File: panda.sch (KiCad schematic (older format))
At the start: 26 parts, among them J1 USB, J2 ICSP, U1 ATMEGA328-P, U2 MAX7219, Y1 12MHz

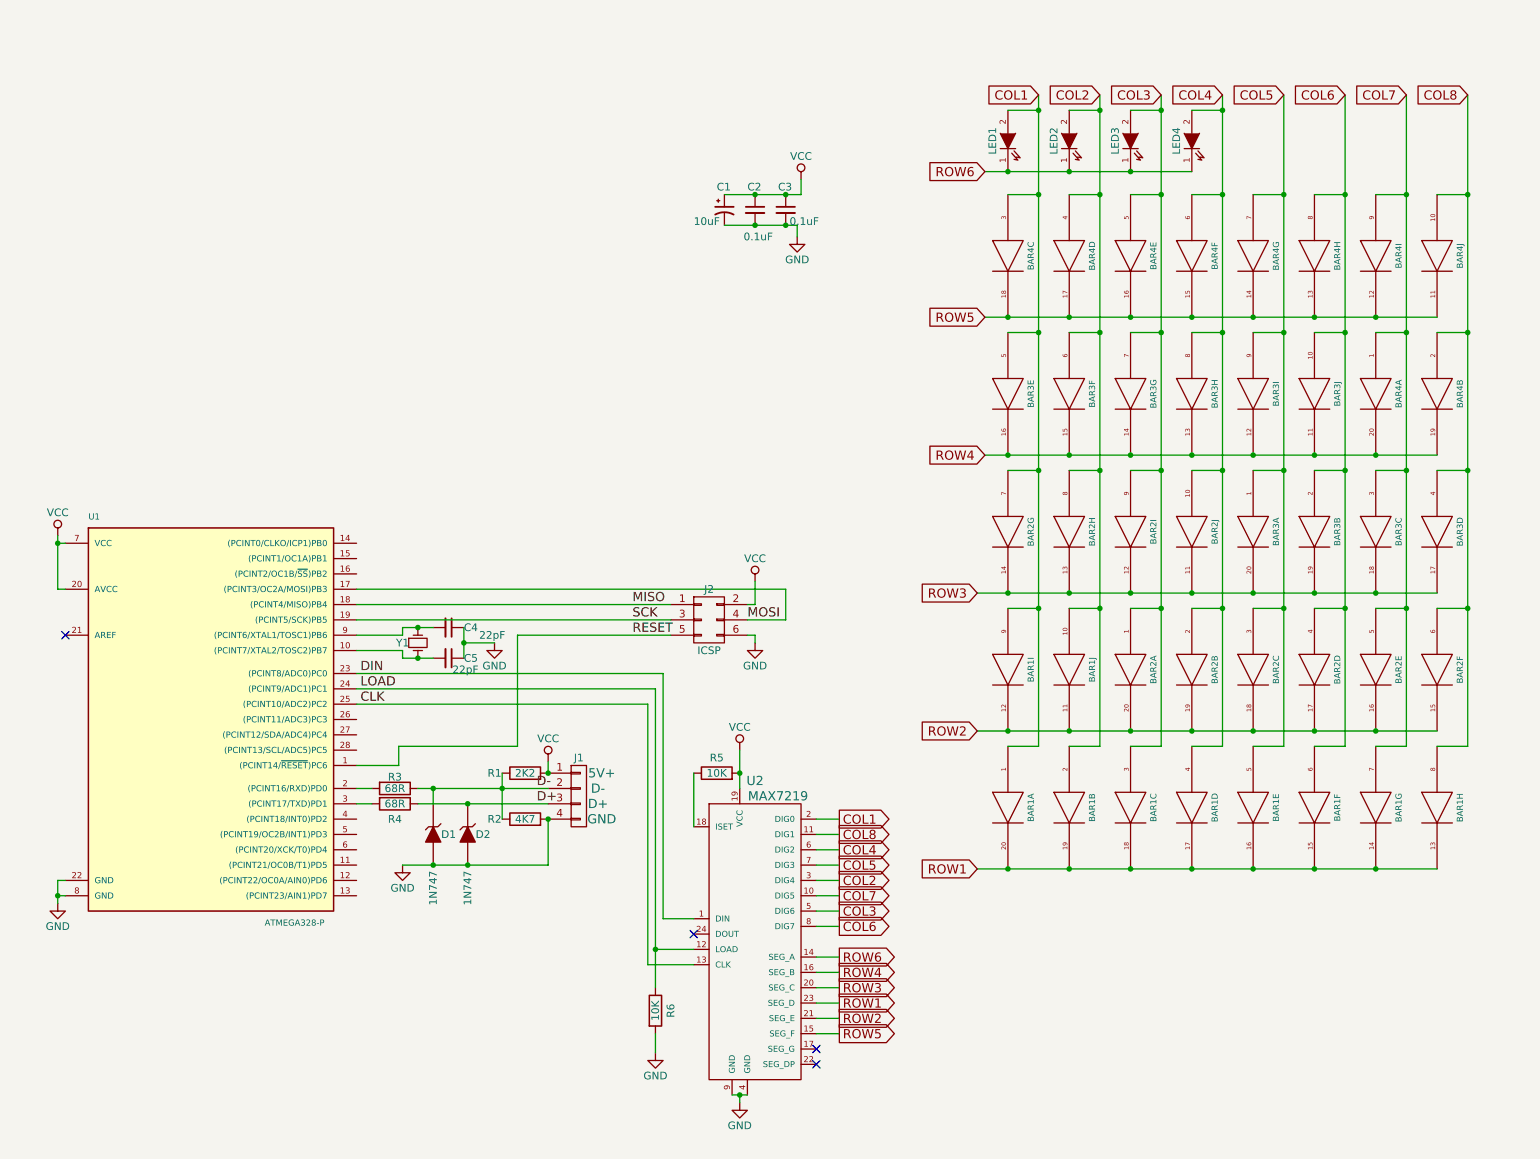
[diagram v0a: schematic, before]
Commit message: Variant with two rows of LED bars.
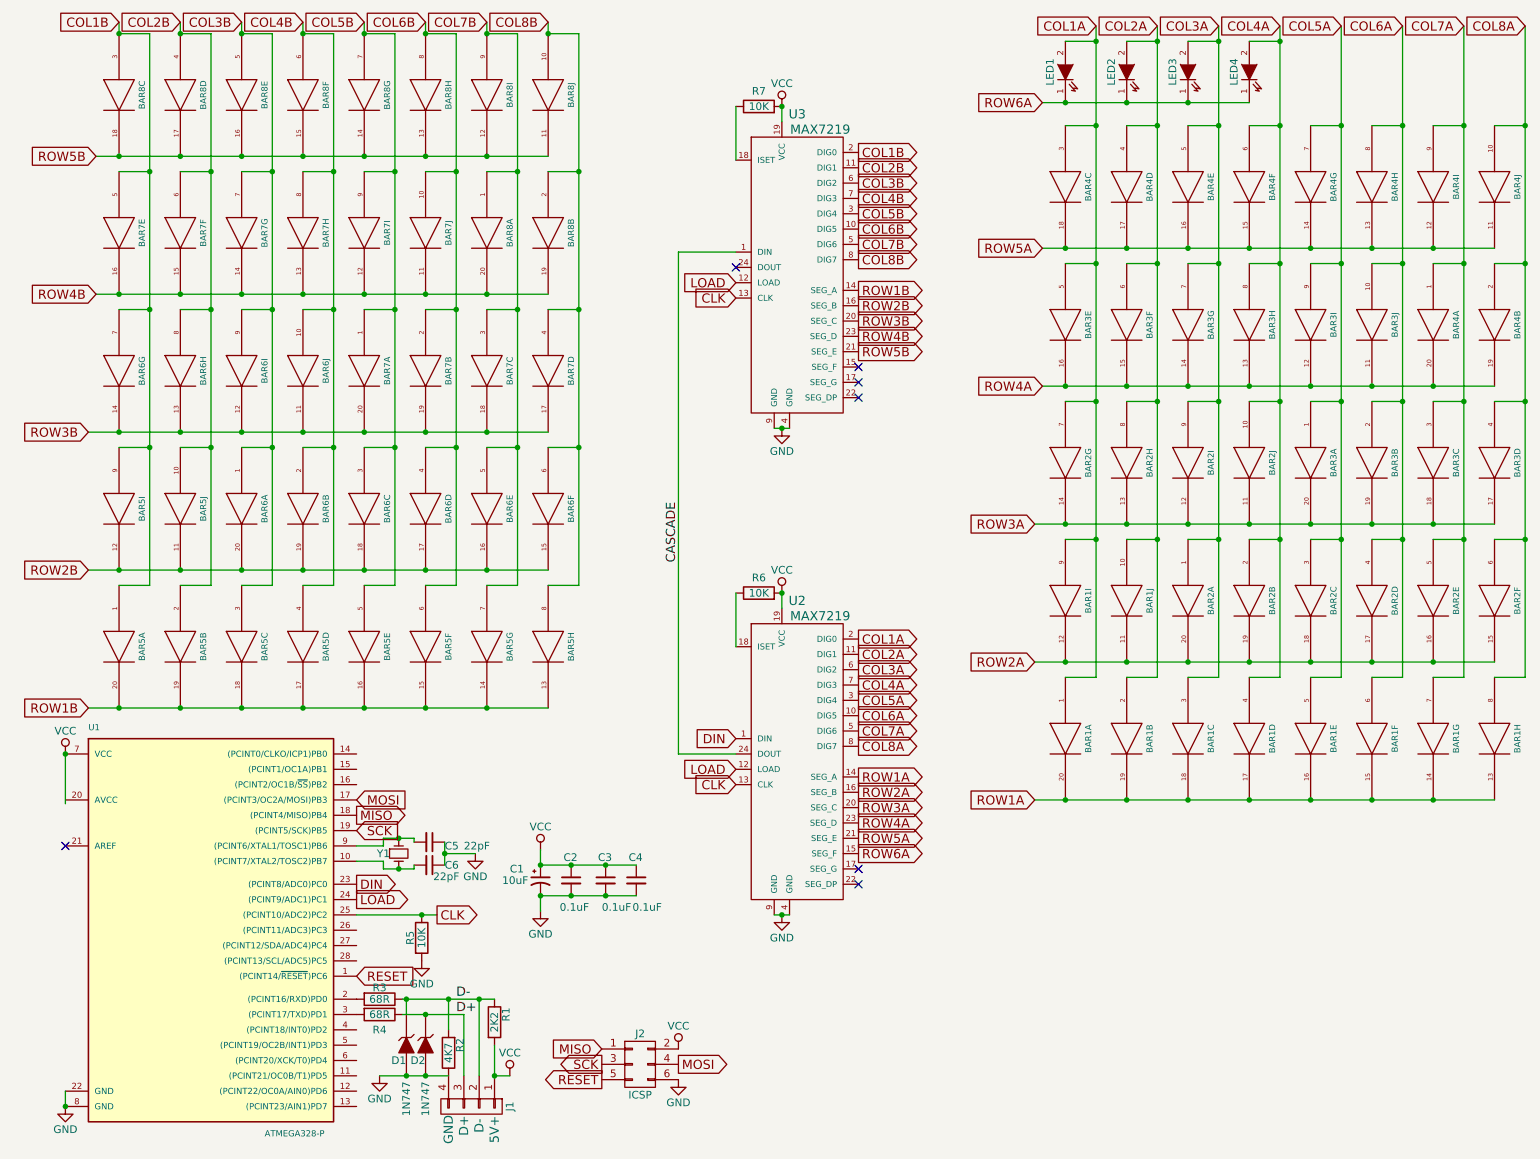
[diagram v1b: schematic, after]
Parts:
- added BAR5, BAR6, BAR7, BAR8: DOT-BAR, Housings_DIP:DIP-20_W7.62mm, symbol DOT-BAR
- added C4: 0.1uF, Capacitors_ThroughHole:C_Rect_L4_W2.5_P2.5, symbol C_Small
- added R7: 10K, custom_resistors:Resistor_Horizontal_RM7.62mm, symbol R
- added U3: MAX7219, Housings_DIP:DIP-24_W7.62mm, symbol MAX7219
- renumbered C4 to C5, C5 to C6, R6 to R5, R5 to R6
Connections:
- net CLK: now also R5.1, U3.13 (CLK)
- net D-: now also R2.2; no longer R2.1
- net GND: now also R2.1, C4.2, U3.4 (GND), U3.9 (GND); no longer R2.2
- net LOAD: now also U3.12 (LOAD); no longer R5.1
- net VCC: now also C4.1, R7.2, U3.19 (VCC); no longer U1.20 (AVCC)
- net CASCADE: now reaches U2.24 (DOUT)
- net CASCADE: now also U3.1 (DIN)
- net COL1 renamed COL1A
- net COL2 renamed COL2A
- net COL2A: now also U2.11 (DIG1); no longer U2.3 (DIG4)
- net COL3 renamed COL3A
- net COL3A: now also U2.6 (DIG2); no longer U2.5 (DIG6)
- net COL4 renamed COL4A
- net COL4A: now also U2.7 (DIG3); no longer U2.6 (DIG2)
- net COL5 renamed COL5A
- net COL5A: now also U2.3 (DIG4); no longer U2.7 (DIG3)
- net COL6 renamed COL6A
- net COL6A: now also U2.10 (DIG5); no longer U2.8 (DIG7)
- net COL7 renamed COL7A
- net COL7A: now also U2.5 (DIG6); no longer U2.10 (DIG5)
- net COL8 renamed COL8A
- net COL8A: now also U2.8 (DIG7); no longer U2.11 (DIG1)
- net ROW1 renamed ROW1A
- net ROW1A: now also U2.14 (SEG_A); no longer U2.23 (SEG_D)
- net ROW2 renamed ROW2A
- net ROW2A: now also U2.16 (SEG_B); no longer U2.21 (SEG_E)
- net ROW3 renamed ROW3A
- net ROW4 renamed ROW4A
- net ROW4A: now also U2.23 (SEG_D); no longer U2.16 (SEG_B)
- net ROW5 renamed ROW5A
- net ROW5A: now also U2.21 (SEG_E); no longer U2.15 (SEG_F)
- net ROW6 renamed ROW6A
- net ROW6A: now also U2.15 (SEG_F); no longer U2.14 (SEG_A)
- new net: R7.1, U3.18 (ISET)
- new net COL1B: BAR5.1 (A), BAR5.9 (A), BAR6.7 (A), BAR7.5 (A), BAR8.3 (A), U3.2 (DIG0)
- new net COL2B: BAR5.10 (A), BAR5.2 (A), BAR6.8 (A), BAR7.6 (A), BAR8.4 (A), U3.11 (DIG1)
- new net COL3B: BAR5.3 (A), BAR6.1 (A), BAR6.9 (A), BAR7.7 (A), BAR8.5 (A), U3.6 (DIG2)
- new net COL4B: BAR5.4 (A), BAR6.10 (A), BAR6.2 (A), BAR7.8 (A), BAR8.6 (A), U3.7 (DIG3)
- new net COL5B: BAR5.5 (A), BAR6.3 (A), BAR7.1 (A), BAR7.9 (A), BAR8.7 (A), U3.3 (DIG4)
- new net COL6B: BAR5.6 (A), BAR6.4 (A), BAR7.10 (A), BAR7.2 (A), BAR8.8 (A), U3.10 (DIG5)
- new net COL7B: BAR5.7 (A), BAR6.5 (A), BAR7.3 (A), BAR8.1 (A), BAR8.9 (A), U3.5 (DIG6)
- new net COL8B: BAR5.8 (A), BAR6.6 (A), BAR7.4 (A), BAR8.10 (A), BAR8.2 (A), U3.8 (DIG7)
- new net ROW1B: BAR5.13 (K), BAR5.14 (K), BAR5.15 (K), BAR5.16 (K), BAR5.17 (K), BAR5.18 (K), BAR5.19 (K), BAR5.20 (K), U3.14 (SEG_A)
- new net ROW2B: BAR5.11 (K), BAR5.12 (K), BAR6.15 (K), BAR6.16 (K), BAR6.17 (K), BAR6.18 (K), BAR6.19 (K), BAR6.20 (K), U3.16 (SEG_B)
- new net ROW3B: BAR6.11 (K), BAR6.12 (K), BAR6.13 (K), BAR6.14 (K), BAR7.17 (K), BAR7.18 (K), BAR7.19 (K), BAR7.20 (K), U3.20 (SEG_C)
- new net ROW4B: BAR7.11 (K), BAR7.12 (K), BAR7.13 (K), BAR7.14 (K), BAR7.15 (K), BAR7.16 (K), BAR8.19 (K), BAR8.20 (K), U3.23 (SEG_D)
- new net ROW5B: BAR8.11 (K), BAR8.12 (K), BAR8.13 (K), BAR8.14 (K), BAR8.15 (K), BAR8.16 (K), BAR8.17 (K), BAR8.18 (K), U3.21 (SEG_E)
- no-connect marks 4 -> 7
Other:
- moved on the sheet: BAR1A, BAR1B, BAR1C, BAR1D, BAR1E, BAR1F, BAR1G, BAR1H, BAR1I, BAR1J, BAR2A, BAR2B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

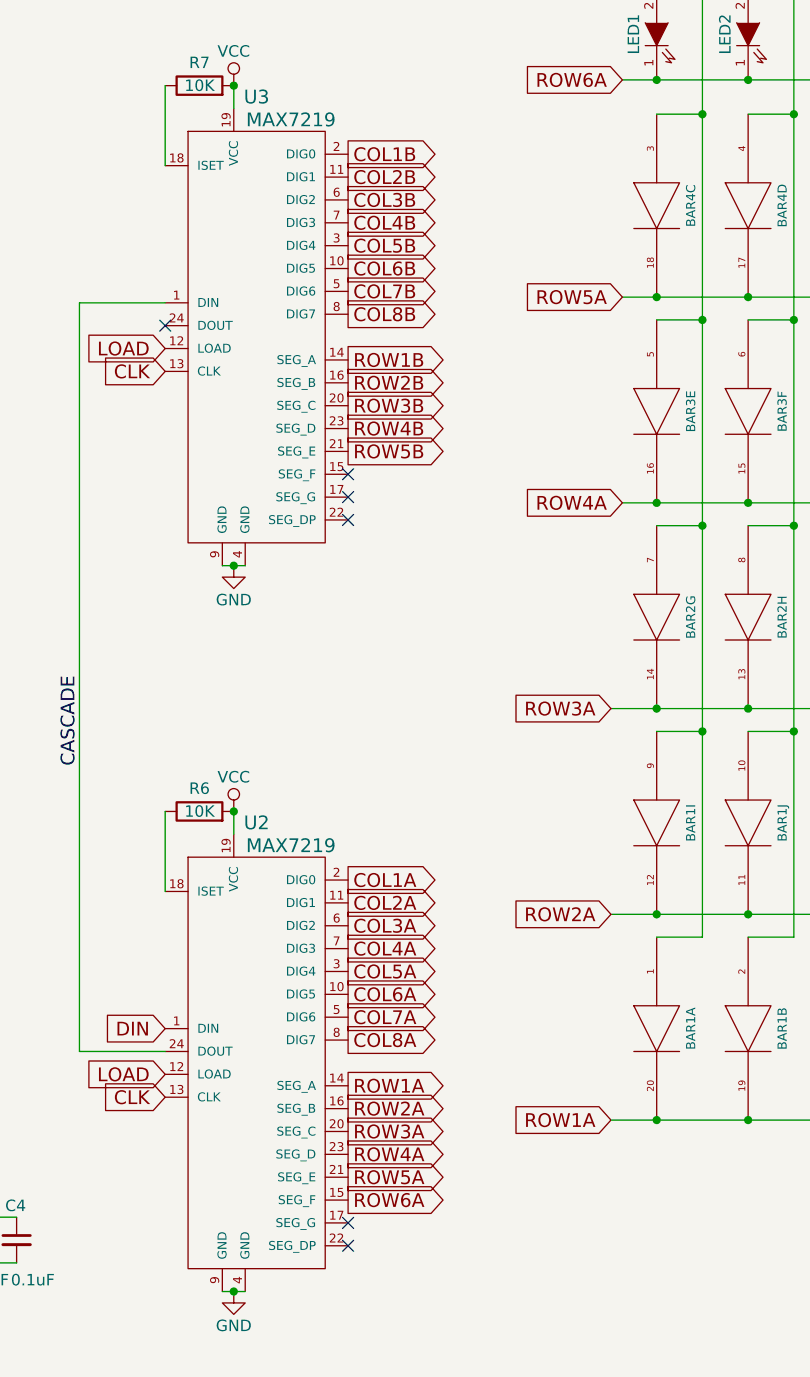
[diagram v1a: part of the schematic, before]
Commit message: Move chips and some other stuff to the back.
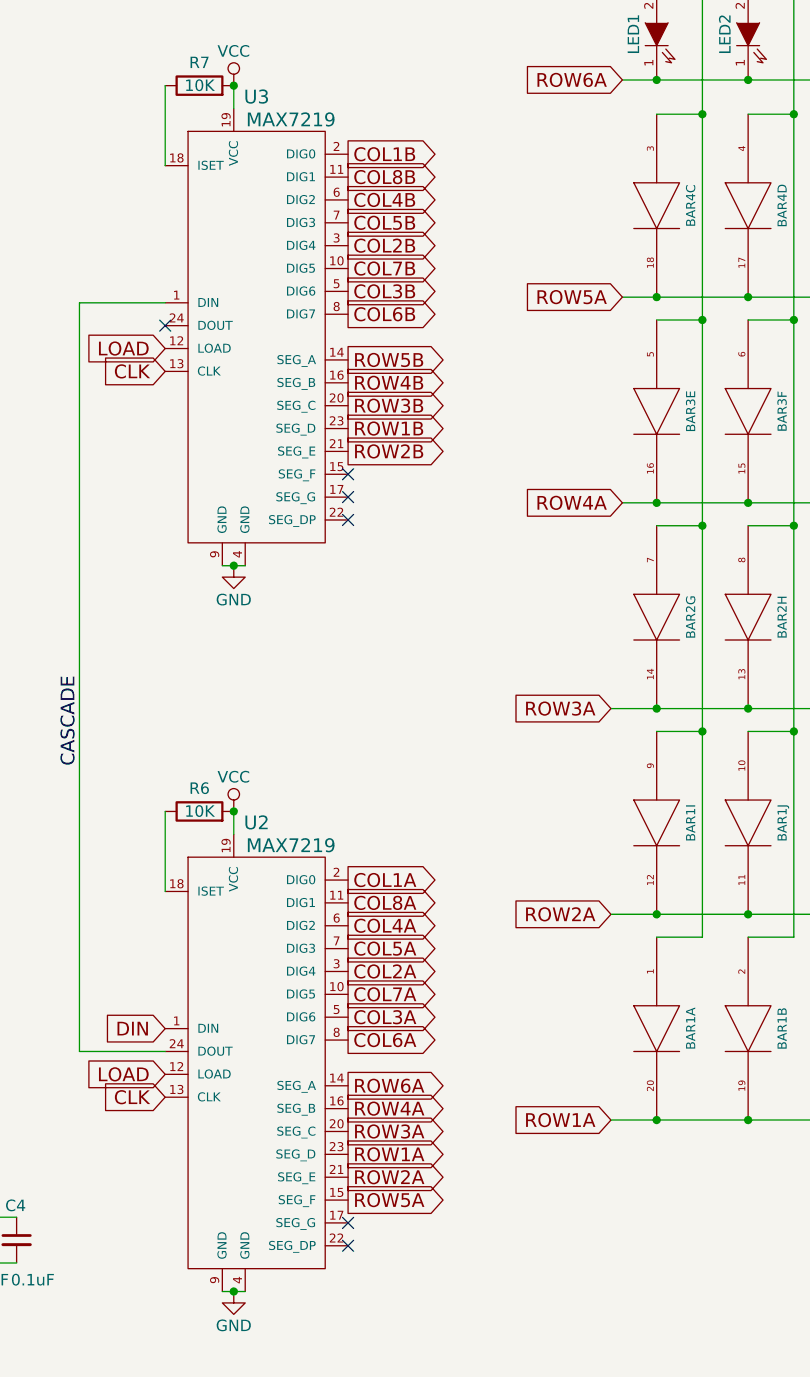
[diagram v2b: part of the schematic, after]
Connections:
- net COL2A: now also U2.3 (DIG4); no longer U2.11 (DIG1)
- net COL2B: now also U3.3 (DIG4); no longer U3.11 (DIG1)
- net COL3A: now also U2.5 (DIG6); no longer U2.6 (DIG2)
- net COL3B: now also U3.5 (DIG6); no longer U3.6 (DIG2)
- net COL4A: now also U2.6 (DIG2); no longer U2.7 (DIG3)
- net COL4B: now also U3.6 (DIG2); no longer U3.7 (DIG3)
- net COL5A: now also U2.7 (DIG3); no longer U2.3 (DIG4)
- net COL5B: now also U3.7 (DIG3); no longer U3.3 (DIG4)
- net COL6A: now also U2.8 (DIG7); no longer U2.10 (DIG5)
- net COL6B: now also U3.8 (DIG7); no longer U3.10 (DIG5)
- net COL7A: now also U2.10 (DIG5); no longer U2.5 (DIG6)
- net COL7B: now also U3.10 (DIG5); no longer U3.5 (DIG6)
- net COL8A: now also U2.11 (DIG1); no longer U2.8 (DIG7)
- net COL8B: now also U3.11 (DIG1); no longer U3.8 (DIG7)
- net ROW1A: now also U2.23 (SEG_D); no longer U2.14 (SEG_A)
- net ROW1B: now also U3.23 (SEG_D); no longer U3.14 (SEG_A)
- net ROW2A: now also U2.21 (SEG_E); no longer U2.16 (SEG_B)
- net ROW2B: now also U3.21 (SEG_E); no longer U3.16 (SEG_B)
- net ROW4A: now also U2.16 (SEG_B); no longer U2.23 (SEG_D)
- net ROW4B: now also U3.16 (SEG_B); no longer U3.23 (SEG_D)
- net ROW5A: now also U2.15 (SEG_F); no longer U2.21 (SEG_E)
- net ROW5B: now also U3.14 (SEG_A); no longer U3.21 (SEG_E)
- net ROW6A: now also U2.14 (SEG_A); no longer U2.15 (SEG_F)
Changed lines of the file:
@@
 Connection ~ 9975 1375
 Connection ~ 10375 1375
-Text GLabel 6025 5625 2    60   Output ~ 0
+Text GLabel 6025 5925 2    60   Output ~ 0
 ROW1A
-Text GLabel 6025 5725 2    60   Output ~ 0
+Text GLabel 6025 6025 2    60   Output ~ 0
 ROW2A
 Text GLabel 6025 5825 2    60   Output ~ 0
 ROW3A
-Text GLabel 6025 5925 2    60   Output ~ 0
+Text GLabel 6025 5725 2    60   Output ~ 0
 ROW4A
-Text GLabel 6025 6025 2    60   Output ~ 0
+Text GLabel 6025 6125 2    60   Output ~ 0
 ROW5A
-Text GLabel 6025 6125 2    60   Output ~ 0
+Text GLabel 6025 5625 2    60   Output ~ 0
 ROW6A
 Wire Wire Line
@@
 Wire Wire Line
 	6025 6125 6025 6125
+Text GLabel 6025 4825 2    60   Output ~ 0
+COL8A
+Wire Wire Line
+	6025 5425 6025 5425
+Text GLabel 6025 5225 2    60   Output ~ 0
+COL7A
+Wire Wire Line
+	6025 5325 6025 5325
 Text GLabel 6025 5425 2    60   Output ~ 0
-COL8A
-Wire Wire Line
-	6025 5425 6025 5425
+COL6A
+Wire Wire Line
+	6025 5225 6025 5225
+Text GLabel 6025 5025 2    60   Output ~ 0
+COL5A
+Wire Wire Line
+	6025 5125 6025 5125
+Text GLabel 6025 4925 2    60   Output ~ 0
+COL4A
+Wire Wire Line
+	6025 5025 6025 5025
 Text GLabel 6025 5325 2    60   Output ~ 0
-COL7A
-Wire Wire Line
-	6025 5325 6025 5325
-Text GLabel 6025 5225 2    60   Output ~ 0
-COL6A
-Wire Wire Line
-	6025 5225 6025 5225
+COL3A
+Wire Wire Line
+	6025 4925 6025 4925
 Text GLabel 6025 5125 2    60   Output ~ 0
-COL5A
-Wire Wire Line
-	6025 5125 6025 5125
-Text GLabel 6025 5025 2    60   Output ~ 0
-COL4A
-Wire Wire Line
-	6025 5025 6025 5025
-Text GLabel 6025 4925 2    60   Output ~ 0
-COL3A
-Wire Wire Line
-	6025 4925 6025 4925
-Text GLabel 6025 4825 2    60   Output ~ 0
 COL2A
 Wire Wire Line
@@
 	1    0    0    -1
 $EndComp
-Text GLabel 6025 2450 2    60   Output ~ 0
+Text GLabel 6025 2750 2    60   Output ~ 0
 ROW1B
-Text GLabel 6025 2550 2    60   Output ~ 0
+Text GLabel 6025 2850 2    60   Output ~ 0
 ROW2B
 Text GLabel 6025 2650 2    60   Output ~ 0
 ROW3B
-Text GLabel 6025 2750 2    60   Output ~ 0
+Text GLabel 6025 2550 2    60   Output ~ 0
 ROW4B
-Text GLabel 6025 2850 2    60   Output ~ 0
+Text GLabel 6025 2450 2    60   Output ~ 0
 ROW5B
 Wire Wire Line
@@
 Wire Wire Line
 	6025 2950 6025 2950
+Text GLabel 6025 1650 2    60   Output ~ 0
+COL8B
+Wire Wire Line
+	6025 2250 6025 2250
+Text GLabel 6025 2050 2    60   Output ~ 0
+COL7B
+Wire Wire Line
+	6025 2150 6025 2150
 Text GLabel 6025 2250 2    60   Output ~ 0
-COL8B
-Wire Wire Line
-	6025 2250 6025 2250
+COL6B
+Wire Wire Line
+	6025 2050 6025 2050
+Text GLabel 6025 1850 2    60   Output ~ 0
+COL5B
+Wire Wire Line
+	6025 1950 6025 1950
+Text GLabel 6025 1750 2    60   Output ~ 0
+COL4B
+Wire Wire Line
+	6025 1850 6025 1850
 Text GLabel 6025 2150 2    60   Output ~ 0
-COL7B
-Wire Wire Line
-	6025 2150 6025 2150
-Text GLabel 6025 2050 2    60   Output ~ 0
-COL6B
-Wire Wire Line
-	6025 2050 6025 2050
+COL3B
+Wire Wire Line
+	6025 1750 6025 1750
 Text GLabel 6025 1950 2    60   Output ~ 0
-COL5B
-Wire Wire Line
-	6025 1950 6025 1950
-Text GLabel 6025 1850 2    60   Output ~ 0
-COL4B
-Wire Wire Line
-	6025 1850 6025 1850
-Text GLabel 6025 1750 2    60   Output ~ 0
-COL3B
-Wire Wire Line
-	6025 1750 6025 1750
-Text GLabel 6025 1650 2    60   Output ~ 0
 COL2B
 Wire Wire Line
